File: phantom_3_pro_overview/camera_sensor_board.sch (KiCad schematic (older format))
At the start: 0 parts

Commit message: Overview: Started work on camera sensor brd.
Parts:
- added U?: Sony EXMOR, CMOS Image Sensor, symbol IC_PQFP48
- added U?: M160A 1511, MPU, symbol IC_PQFP_5_3_5_3
- added U?: TLV62130, Buck conv., symbol LD1117S12CTR
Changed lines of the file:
@@
 LIBS:transistors-switches
 LIBS:transistors-power
+LIBS:sensors-v2
+LIBS:regul-v2
 LIBS:phantom_3_pro_overview-cache
 EELAYER 25 0
 EELAYER END
-$Descr A4 11693 8268
+$Descr User 5197 5118
 encoding utf-8
-Sheet 6 23
+Sheet 23 23
 Title "Overview of the Phantom 3 Pro Camera Sensor board"
 Date ""
@@
 $EndDescr
 Wire Bus Line
-	2900 2300 4000 2300
-Text HLabel 4000 2300 2    60   BiDi ~ 0
+	2150 2400 1050 2400
+Text HLabel 1050 2400 0    60   BiDi ~ 0
 FLAT_TOP
+$Comp
+L IC_PQFP48 U?
+U 1 1 5980D40C
+P 3100 1500
+F 0 "U?" H 3100 1400 50  0001 C CNN
+F 1 "Sony EXMOR" H 3100 1600 50  0000 C CNN
+F 2 "CMOS Image Sensor" H 3100 1500 50  0000 C CNN
+F 3 "DOCUMENTATION" H 3100 1500 50  0001 C CNN
+	1    3100 1500
+	1    0    0    -1
+$EndComp
+$Comp
+L IC_PQFP_5_3_5_3 U?
+U 1 1 5980DD95
+P 2300 2900
+F 0 "U?" H 2300 2700 50  0001 C CNN
+F 1 "M160A 1511" H 2300 3000 50  0000 C CNN
+F 2 "MPU" H 2300 2900 50  0000 C CNN
+F 3 "DOCUMENTATION" H 2300 2800 50  0001 C CNN
+	1    2300 2900
+	1    0    0    -1
+$EndComp
+$Comp
+L LD1117S12CTR U?
+U 1 1 5980ED4D
+P 3750 2950
+F 0 "U?" H 3750 3200 50  0001 C CNN
+F 1 "TLV62130" H 3750 3150 50  0000 C CNN
+F 2 "Buck conv." H 3750 3050 50  0000 C CNN
+F 3 "" H 3750 2950 50  0001 C CNN
+	1    3750 2950
+	1    0    0    -1
+$EndComp
+Entry Wire Line
+	3850 950  3950 1050
+Entry Wire Line
+	3850 1050 3950 1150
+Entry Wire Line
+	3850 1150 3950 1250
+Entry Wire Line
+	3850 1250 3950 1350
+Entry Wire Line
+	3850 1350 3950 1450
+Entry Wire Line
+	3850 1450 3950 1550
+Entry Wire Line
+	3850 1550 3950 1650
+Entry Wire Line
+	3850 1650 3950 1750
+Entry Wire Line
+	3850 1750 3950 1850
+Entry Wire Line
+	3850 1850 3950 1950
+Entry Wire Line
+	3850 1950 3950 2050
+Entry Wire Line
+	3850 2050 3950 2150
+Wire Wire Line
+	3800 950  3850 950
+Wire Wire Line
+	3850 1050 3800 1050
+Wire Wire Line
+	3800 1150 3850 1150
+Wire Wire Line
+	3850 1250 3800 1250
+Wire Wire Line
+	3800 1350 3850 1350
+Wire Wire Line
+	3800 1450 3850 1450
+Wire Wire Line
+	3850 1550 3800 1550
+Wire Wire Line
+	3800 1650 3850 1650
+Wire Wire Line
+	3850 1750 3800 1750
+Wire Wire Line
+	3800 1850 3850 1850
+Wire Wire Line
+	3850 1950 3800 1950
+Wire Wire Line
+	3800 2050 3850 2050
+Entry Wire Line
+	2550 750  2650 650
+Entry Wire Line
+	2650 750  2750 650
+Entry Wire Line
+	2750 750  2850 650
+Entry Wire Line
+	2850 750  2950 650
+Entry Wire Line
+	2950 750  3050 650
+Entry Wire Line
+	3050 750  3150 650
+Entry Wire Line
+	3150 750  3250 650
+Entry Wire Line
+	3250 750  3350 650
+Entry Wire Line
+	3350 750  3450 650
+Entry Wire Line
+	3450 750  3550 650
+Entry Wire Line
+	3550 750  3650 650
+Entry Wire Line
+	3650 750  3750 650
+Wire Wire Line
+	2550 800  2550 750
+Wire Wire Line
+	2650 750  2650 800
+Wire Wire Line
+	2750 800  2750 750
+Wire Wire Line
+	2850 750  2850 800
+Wire Wire Line
+	2950 800  2950 750
+Wire Wire Line
+	3050 800  3050 750
+Wire Wire Line
+	3150 750  3150 800
+Wire Wire Line
+	3250 800  3250 750
+Wire Wire Line
+	3350 750  3350 800
+Wire Wire Line
+	3450 800  3450 750
+Wire Wire Line
+	3550 750  3550 800
+Wire Wire Line
+	3650 800  3650 750
+Entry Wire Line
+	2350 950  2250 1050
+Entry Wire Line
+	2350 1050 2250 1150
+Entry Wire Line
+	2350 1150 2250 1250
+Entry Wire Line
+	2350 1250 2250 1350
+Entry Wire Line
+	2350 1350 2250 1450
+Entry Wire Line
+	2350 1450 2250 1550
+Entry Wire Line
+	2350 1550 2250 1650
+Entry Wire Line
+	2350 1650 2250 1750
+Entry Wire Line
+	2350 1750 2250 1850
+Entry Wire Line
+	2350 1850 2250 1950
+Entry Wire Line
+	2350 1950 2250 2050
+Entry Wire Line
+	2350 2050 2250 2150
+Wire Wire Line
+	2400 950  2350 950
+Wire Wire Line
+	2350 1050 2400 1050
+Wire Wire Line
+	2400 1150 2350 1150
+Wire Wire Line
+	2350 1250 2400 1250
+Wire Wire Line
+	2400 1350 2350 1350
+Wire Wire Line
+	2400 1450 2350 1450
+Wire Wire Line
+	2350 1550 2400 1550
+Wire Wire Line
+	2400 1650 2350 1650
+Wire Wire Line
+	2350 1750 2400 1750
+Wire Wire Line
+	2400 1850 2350 1850
+Wire Wire Line
+	2350 1950 2400 1950
+Wire Wire Line
+	2400 2050 2350 2050
+Entry Wire Line
+	2550 2250 2650 2350
+Entry Wire Line
+	2650 2250 2750 2350
+Entry Wire Line
+	2750 2250 2850 2350
+Entry Wire Line
+	2850 2250 2950 2350
+Entry Wire Line
+	2950 2250 3050 2350
+Entry Wire Line
+	3050 2250 3150 2350
+Entry Wire Line
+	3150 2250 3250 2350
+Entry Wire Line
+	3250 2250 3350 2350
+Entry Wire Line
+	3350 2250 3450 2350
+Entry Wire Line
+	3450 2250 3550 2350
+Entry Wire Line
+	3550 2250 3650 2350
+Entry Wire Line
+	3650 2250 3750 2350
+Wire Wire Line
+	2550 2200 2550 2250
+Wire Wire Line
+	2650 2250 2650 2200
+Wire Wire Line
+	2750 2200 2750 2250
+Wire Wire Line
+	2850 2250 2850 2200
+Wire Wire Line
+	2950 2200 2950 2250
+Wire Wire Line
+	3050 2200 3050 2250
+Wire Wire Line
+	3150 2250 3150 2200
+Wire Wire Line
+	3250 2200 3250 2250
+Wire Wire Line
+	3350 2250 3350 2200
+Wire Wire Line
+	3450 2200 3450 2250
+Wire Wire Line
+	3550 2250 3550 2200
+Wire Wire Line
+	3650 2200 3650 2250
 $EndSCHEMATC

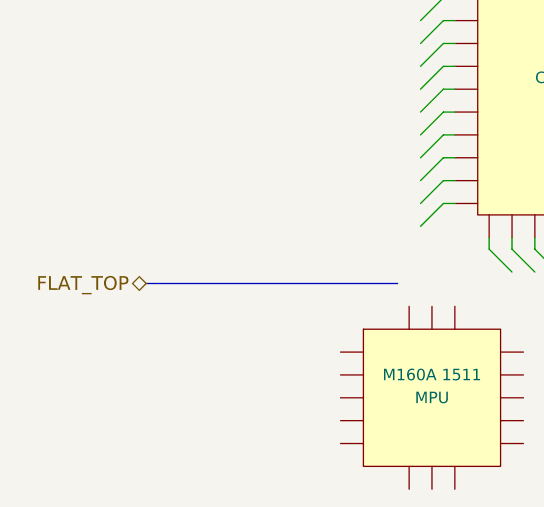
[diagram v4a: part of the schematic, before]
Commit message: Overview: Updated to latest findings.
Added magnetometer to gimbal control, and made some minor fixes.
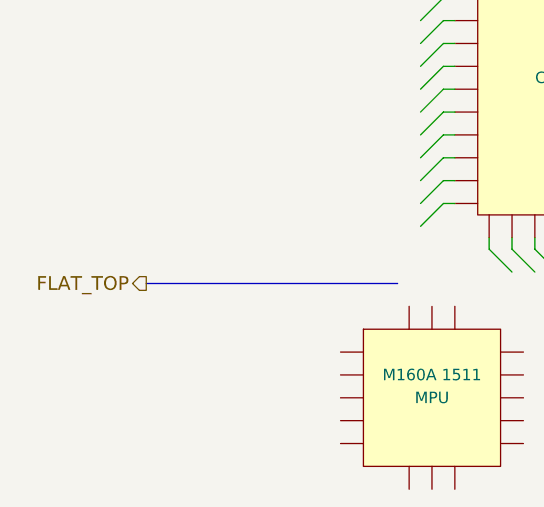
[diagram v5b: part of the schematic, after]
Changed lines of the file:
@@
 Wire Bus Line
 	2150 2400 1050 2400
-Text HLabel 1050 2400 0    60   BiDi ~ 0
+Text HLabel 1050 2400 0    60   Output ~ 0
 FLAT_TOP
 $Comp

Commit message: Overview: Upgraded to KiCAD 5.0.1.
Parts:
- U?: symbol IC_PQFP48 -> ic_dil_generic:IC_PQFP48
- U?: symbol IC_PQFP_5_3_5_3 -> ic_dil_generic:IC_PQFP_5_3_5_3
- U?: symbol LD1117S12CTR -> phantom_3_pro_overview-rescue:LD1117S12CTR
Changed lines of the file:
@@
-EESchema Schematic File Version 2
-LIBS:power
-LIBS:device
-LIBS:transistors
-LIBS:conn
-LIBS:linear
-LIBS:regul
-LIBS:74xx
-LIBS:cmos4000
-LIBS:adc-dac
-LIBS:memory
-LIBS:xilinx
-LIBS:microcontrollers
-LIBS:dsp
-LIBS:microchip
-LIBS:analog_switches
-LIBS:motorola
-LIBS:texas
-LIBS:intel
-LIBS:audio
-LIBS:interface
-LIBS:digital-audio
-LIBS:philips
-LIBS:display
-LIBS:cypress
-LIBS:siliconi
-LIBS:opto
-LIBS:atmel
-LIBS:contrib
-LIBS:valves
-LIBS:motors
-LIBS:ic_dil_generic
-LIBS:sensors
-LIBS:u-blox
-LIBS:amplifiers
-LIBS:transistors-switches
-LIBS:transistors-power
-LIBS:sensors-v2
-LIBS:regul-v2
+EESchema Schematic File Version 4
 LIBS:phantom_3_pro_overview-cache
-EELAYER 25 0
+EELAYER 26 0
 EELAYER END
 $Descr User 5197 5118
@@
 FLAT_TOP
 $Comp
-L IC_PQFP48 U?
+L ic_dil_generic:IC_PQFP48 U?
 U 1 1 5980D40C
 P 3100 1500
@@
 $EndComp
 $Comp
-L IC_PQFP_5_3_5_3 U?
+L ic_dil_generic:IC_PQFP_5_3_5_3 U?
 U 1 1 5980DD95
 P 2300 2900
@@
 $EndComp
 $Comp
-L LD1117S12CTR U?
+L phantom_3_pro_overview-rescue:LD1117S12CTR U?
 U 1 1 5980ED4D
 P 3750 2950

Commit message: All: Finished updating to KiCad 5.0.1.
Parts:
- U?: symbol phantom_3_pro_overview-rescue:LD1117S12CTR -> Regulator_Linear:LD1117S12TR_SOT223
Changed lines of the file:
@@
 $EndComp
 $Comp
-L phantom_3_pro_overview-rescue:LD1117S12CTR U?
+L Regulator_Linear:LD1117S12TR_SOT223 U?
 U 1 1 5980ED4D
 P 3750 2950
 F 0 "U?" H 3750 3200 50  0001 C CNN
-F 1 "TLV62130" H 3750 3150 50  0000 C CNN
+F 1 "TLV62130" H 3750 3100 50  0000 C CNN
 F 2 "Buck conv." H 3750 3050 50  0000 C CNN
 F 3 "" H 3750 2950 50  0001 C CNN
